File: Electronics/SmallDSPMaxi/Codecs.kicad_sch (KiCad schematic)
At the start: 72 parts, among them J1 IDC Header

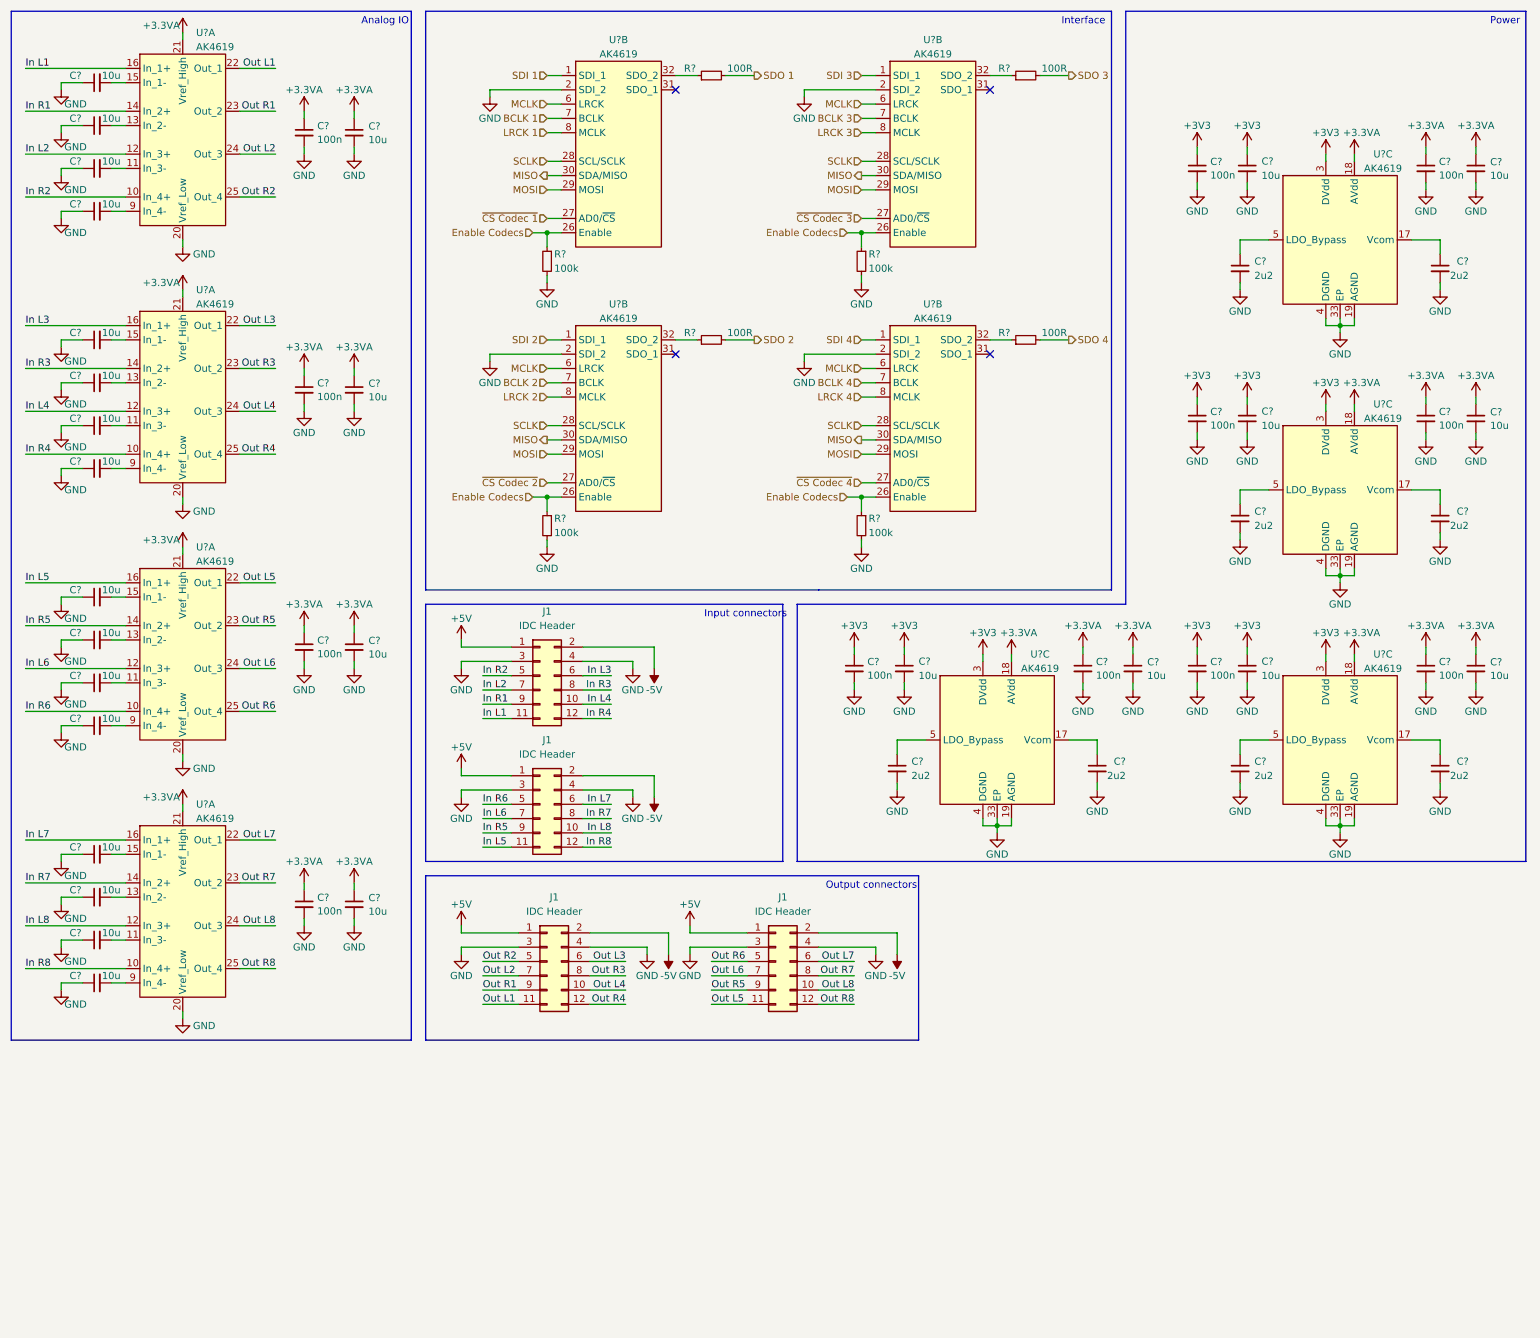
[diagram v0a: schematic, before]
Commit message: Finishes SmallDSP Maxi plus the fitting In- and Output Boards
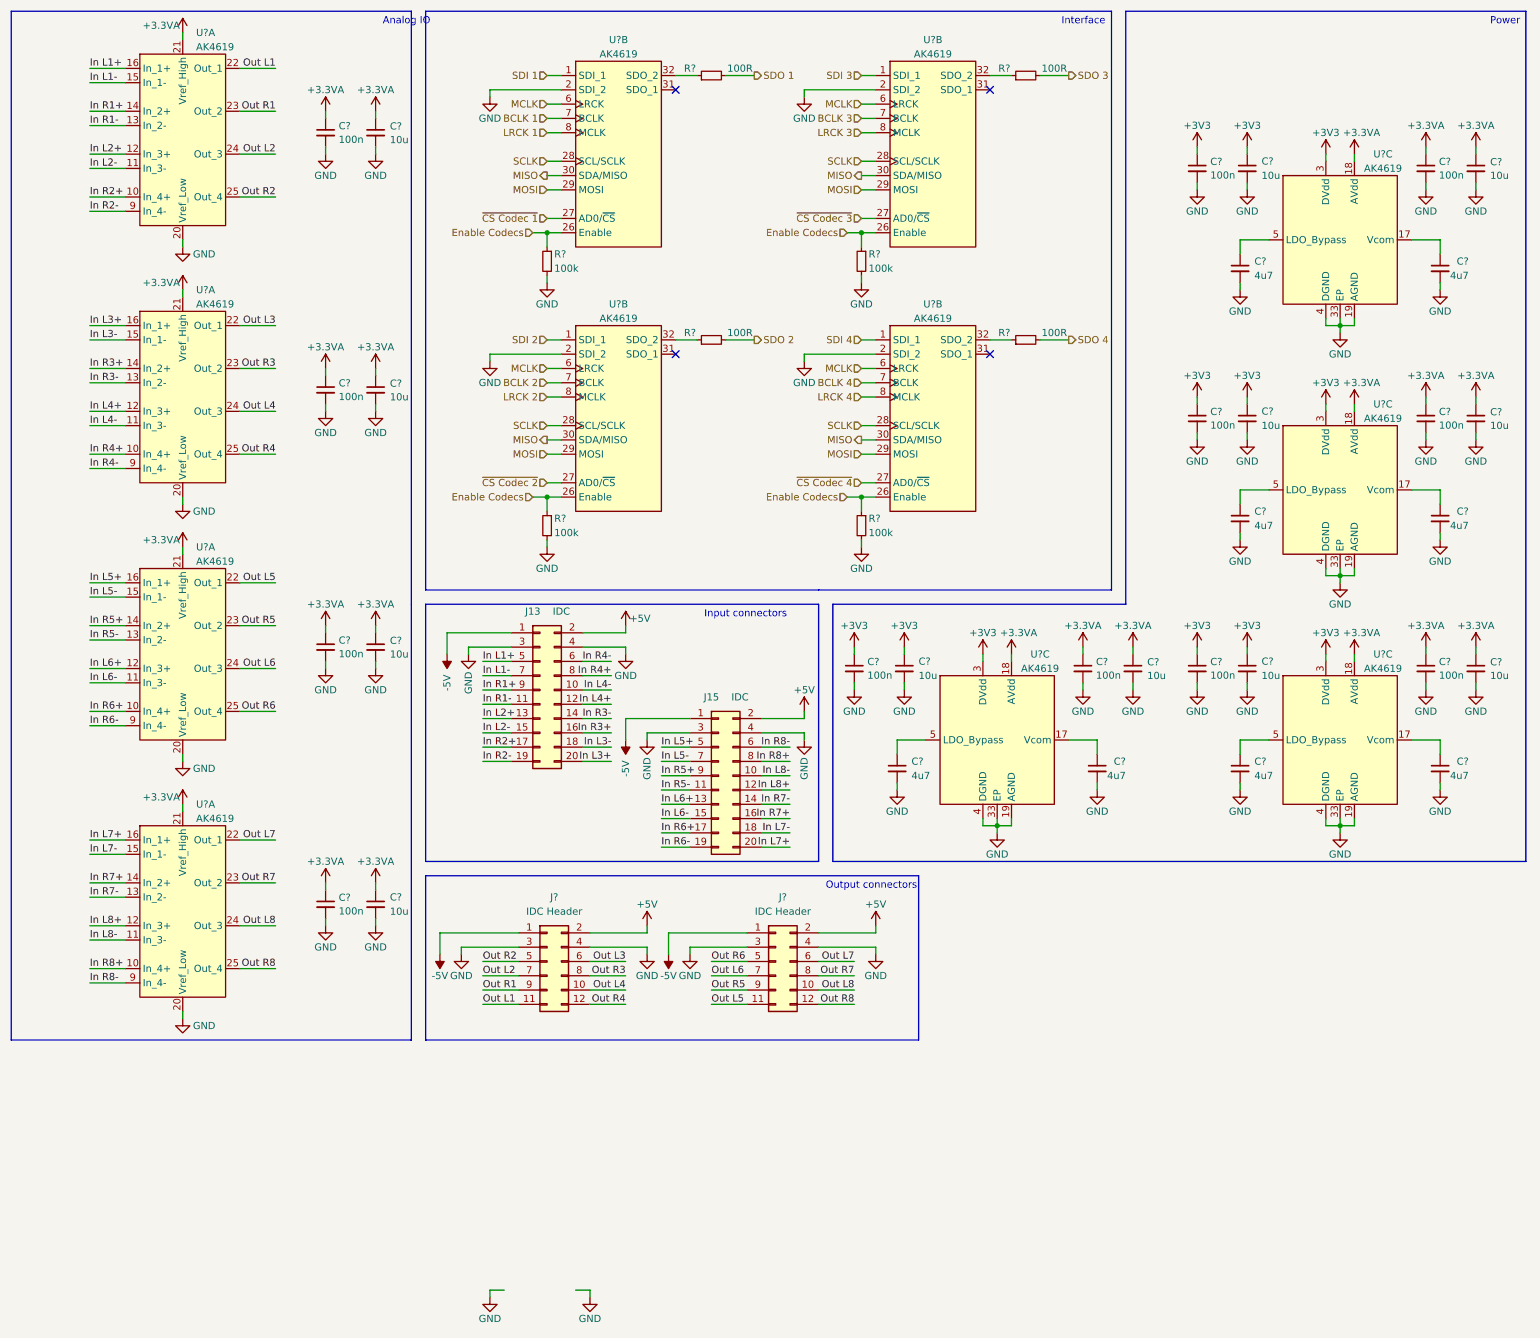
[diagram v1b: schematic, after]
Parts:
- removed C? (x16): 10u, Capacitor_SMD:C_1206_3216Metric, symbol Device:C_Small
- removed J1 (x2): IDC Header, Connector_IDC:IDC-Header_2x06_P2.54mm_Vertical, symbol Connector_Generic:Conn_02x06_Odd_Even
- added J13, J15: IDC, Connector_IDC:IDC-Header_2x10_P2.54mm_Vertical, symbol Connector_Generic:Conn_02x10_Odd_Even
- C? (x12): JLC Part Number C307331 -> (none); LCSC Part # (none) -> C307331
- C? (x12): JLC Part Number C96446 -> (none); LCSC Part # (none) -> C96446
- C? (x8): value 2u2 -> 4u7; footprint Capacitor_SMD:C_0805_2012Metric -> Capacitor_SMD:C_0603_1608Metric; JLC Part Number C377773 -> (none); LCSC Part # (none) -> C19666; Notes (none) -> -50%@3.3V and 0Vrms; Part Number CL21A225KBQNNNE -> CL10A475KO8NNNC
- J? (x2): renamed from J1; JLC Part Number - -> (none); LCSC Part # (none) -> -
- R? (x4): JLC Part Number C25076 -> (none); LCSC Part # (none) -> C25076
- R? (x4): JLC Part Number C25741 -> (none); LCSC Part # (none) -> C25741
- U? (x12): LCSC Part # (none) -> -
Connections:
- net +5V: now also J?.2 (Pin_2), J?.2 (Pin_2), J13.2 (Pin_2), J15.2 (Pin_2); no longer J?.1 (Pin_1), J?.1 (Pin_1)
- net -5V: now also J?.1 (Pin_1), J?.1 (Pin_1), J13.1 (Pin_1), J15.1 (Pin_1); no longer J?.2 (Pin_2), J?.2 (Pin_2)
- net GND: now also J13.3 (Pin_3), J13.4 (Pin_4), J15.3 (Pin_3), J15.4 (Pin_4)
- net In L6-: now reaches U?.11 (In_3-)
- net In L6-: now also J15.15 (Pin_15)
- net In R5-: now reaches U?.13 (In_2-)
- net In R5-: now also J15.11 (Pin_11)
- net In L5-: now reaches U?.15 (In_1-)
- net In L5-: now also J15.7 (Pin_7)
- net In R6-: now reaches U?.9 (In_4-)
- net In R6-: now also J15.19 (Pin_19)
- net In L2-: now reaches U?.11 (In_3-)
- net In L2-: now also J13.15 (Pin_15)
- net In L1-: now reaches U?.15 (In_1-)
- net In L1-: now also J13.7 (Pin_7)
- net In L8-: now reaches U?.11 (In_3-)
- net In L8-: now also J15.10 (Pin_10)
- net In R1-: now reaches U?.13 (In_2-)
- net In R1-: now also J13.11 (Pin_11)
- net In R2-: now reaches U?.9 (In_4-)
- net In R2-: now also J13.19 (Pin_19)
- net In L3-: now reaches U?.15 (In_1-)
- net In L3-: now also J13.18 (Pin_18)
- net In R7-: now reaches U?.13 (In_2-)
- net In R7-: now also J15.14 (Pin_14)
- net In R3-: now reaches U?.13 (In_2-)
- net In R3-: now also J13.14 (Pin_14)
- net In R8-: now reaches U?.9 (In_4-)
- net In R8-: now also J15.6 (Pin_6)
- net In L4-: now reaches U?.11 (In_3-)
- net In L4-: now also J13.10 (Pin_10)
- net In R4-: now reaches U?.9 (In_4-)
- net In R4-: now also J13.6 (Pin_6)
- net In L7-: now reaches U?.15 (In_1-)
- net In L7-: now also J15.18 (Pin_18)
- net In L1 renamed In L1+
- net In L1+: now also J13.5 (Pin_5)
- net In L2 renamed In L2+
- net In L2+: now also J13.13 (Pin_13)
- net In L3 renamed In L3+
- net In L3+: now also J13.20 (Pin_20)
- net In L4 renamed In L4+
- net In L4+: now also J13.12 (Pin_12)
- net In L5 renamed In L5+
- net In L5+: now also J15.5 (Pin_5)
- net In L6 renamed In L6+
- net In L6+: now also J15.13 (Pin_13)
- net In L7 renamed In L7+
- net In L7+: now also J15.20 (Pin_20)
- net In L8 renamed In L8+
- net In L8+: now also J15.12 (Pin_12)
- net In R1 renamed In R1+
- net In R1+: now also J13.9 (Pin_9)
- net In R2 renamed In R2+
- net In R2+: now also J13.17 (Pin_17)
- net In R3 renamed In R3+
- net In R3+: now also J13.16 (Pin_16)
- net In R4 renamed In R4+
- net In R4+: now also J13.8 (Pin_8)
- net In R5 renamed In R5+
- net In R5+: now also J15.9 (Pin_9)
- net In R6 renamed In R6+
- net In R6+: now also J15.17 (Pin_17)
- net In R7 renamed In R7+
- net In R7+: now also J15.16 (Pin_16)
- net In R8 renamed In R8+
- net In R8+: now also J15.8 (Pin_8)
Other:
- moved on the sheet: C?

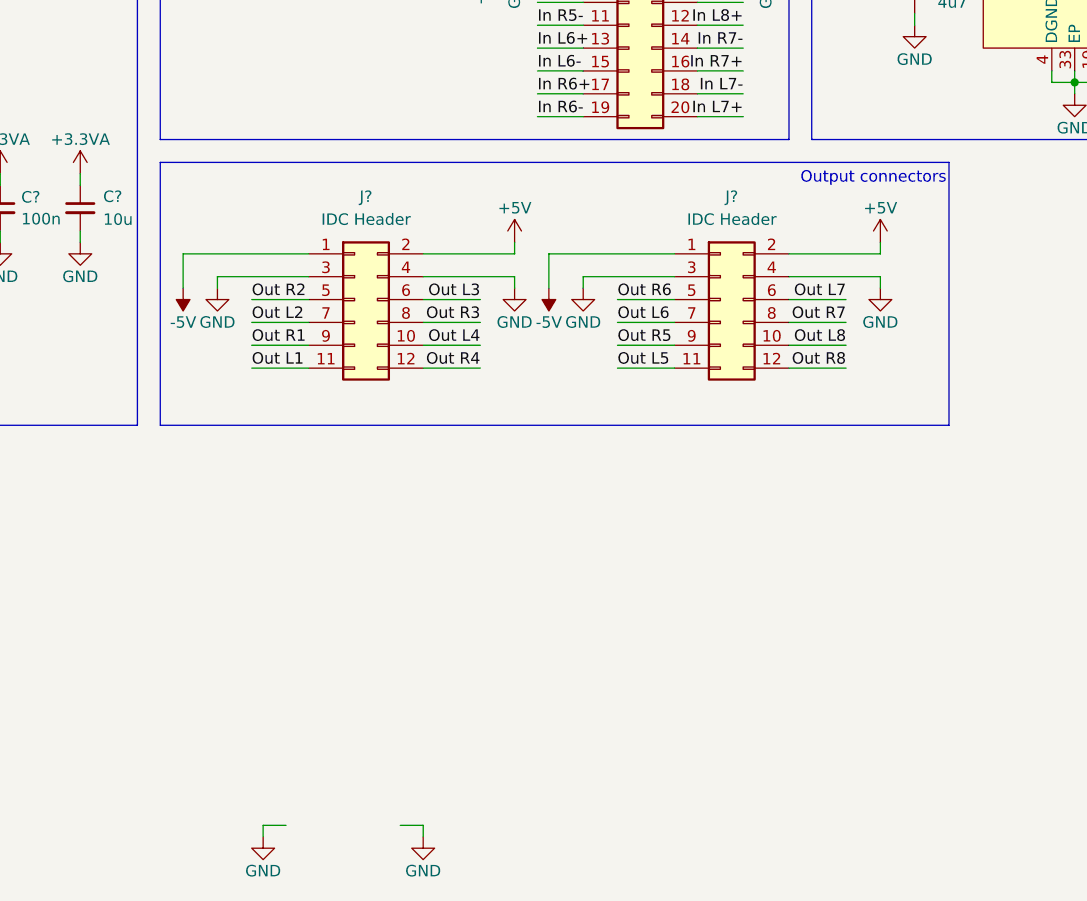
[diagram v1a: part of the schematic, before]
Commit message: replaces 12pin IDC out header with 14pin one because of better availability.
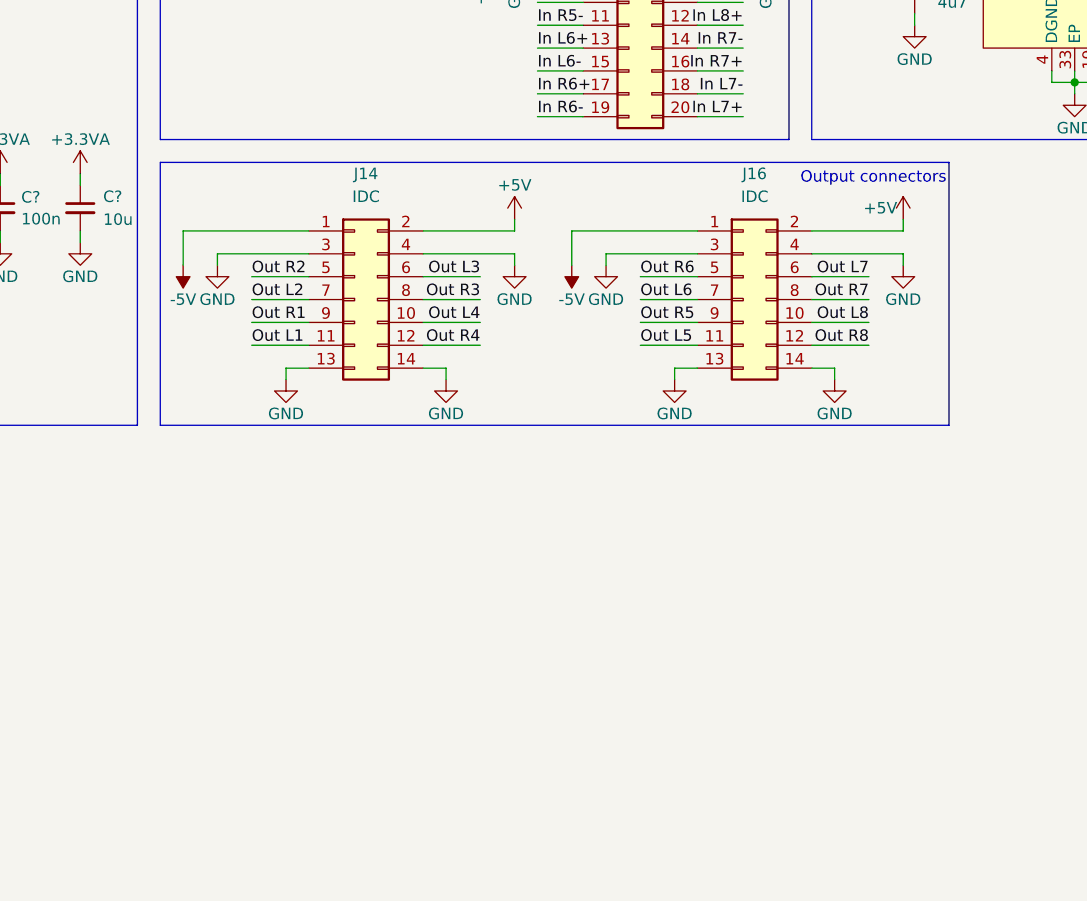
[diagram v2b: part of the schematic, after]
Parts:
- removed J? (x2): IDC Header, Connector_IDC:IDC-Header_2x06_P2.54mm_Vertical, symbol Connector_Generic:Conn_02x06_Odd_Even
- added J14, J16: IDC, Connector_IDC:IDC-Header_2x07_P2.54mm_Vertical, symbol Connector_Generic:Conn_02x07_Odd_Even
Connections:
- net +5V: now also J14.2 (Pin_2), J16.2 (Pin_2)
- net -5V: now also J14.1 (Pin_1), J16.1 (Pin_1)
- net GND: now also J14.13 (Pin_13), J14.14 (Pin_14), J14.3 (Pin_3), J14.4 (Pin_4), J16.13 (Pin_13), J16.14 (Pin_14), J16.3 (Pin_3), J16.4 (Pin_4)
- net Out L1: now also J14.11 (Pin_11)
- net Out L2: now also J14.7 (Pin_7)
- net Out L3: now also J14.6 (Pin_6)
- net Out L4: now also J14.10 (Pin_10)
- net Out L5: now also J16.11 (Pin_11)
- net Out L6: now also J16.7 (Pin_7)
- net Out L7: now also J16.6 (Pin_6)
- net Out L8: now also J16.10 (Pin_10)
- net Out R1: now also J14.9 (Pin_9)
- net Out R2: now also J14.5 (Pin_5)
- net Out R3: now also J14.8 (Pin_8)
- net Out R4: now also J14.12 (Pin_12)
- net Out R5: now also J16.9 (Pin_9)
- net Out R6: now also J16.5 (Pin_5)
- net Out R7: now also J16.8 (Pin_8)
- net Out R8: now also J16.12 (Pin_12)

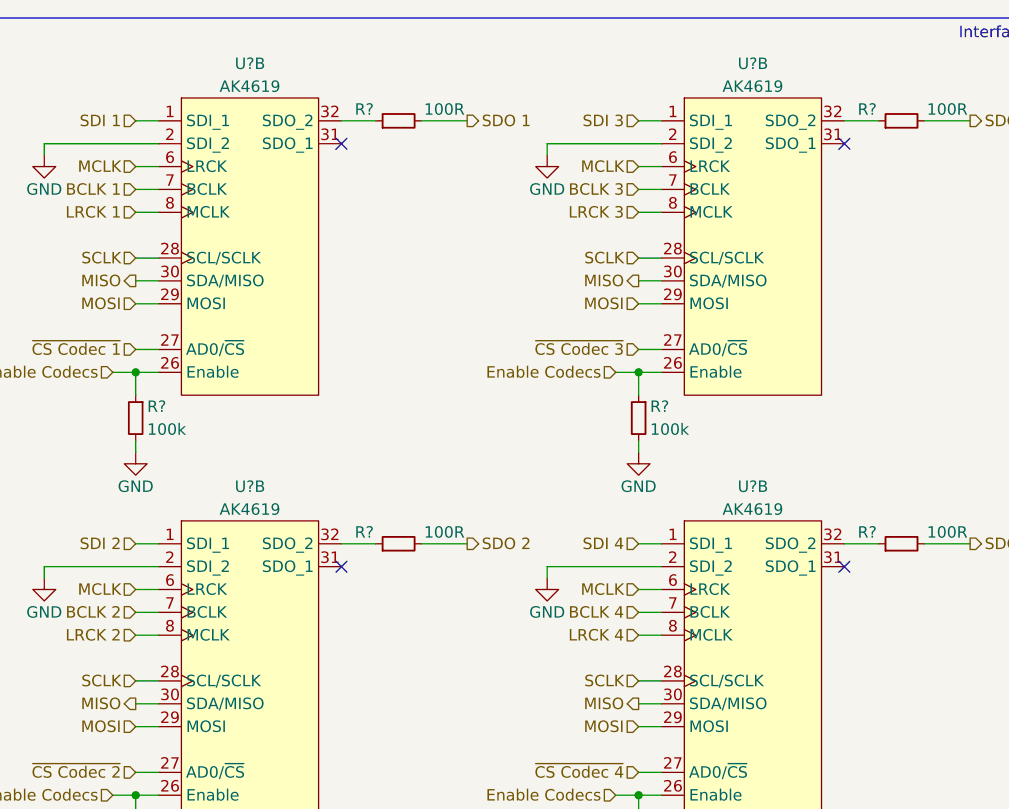
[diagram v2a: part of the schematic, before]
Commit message: Fixes schematic mistakes, like incorrect routin of clock to codecs
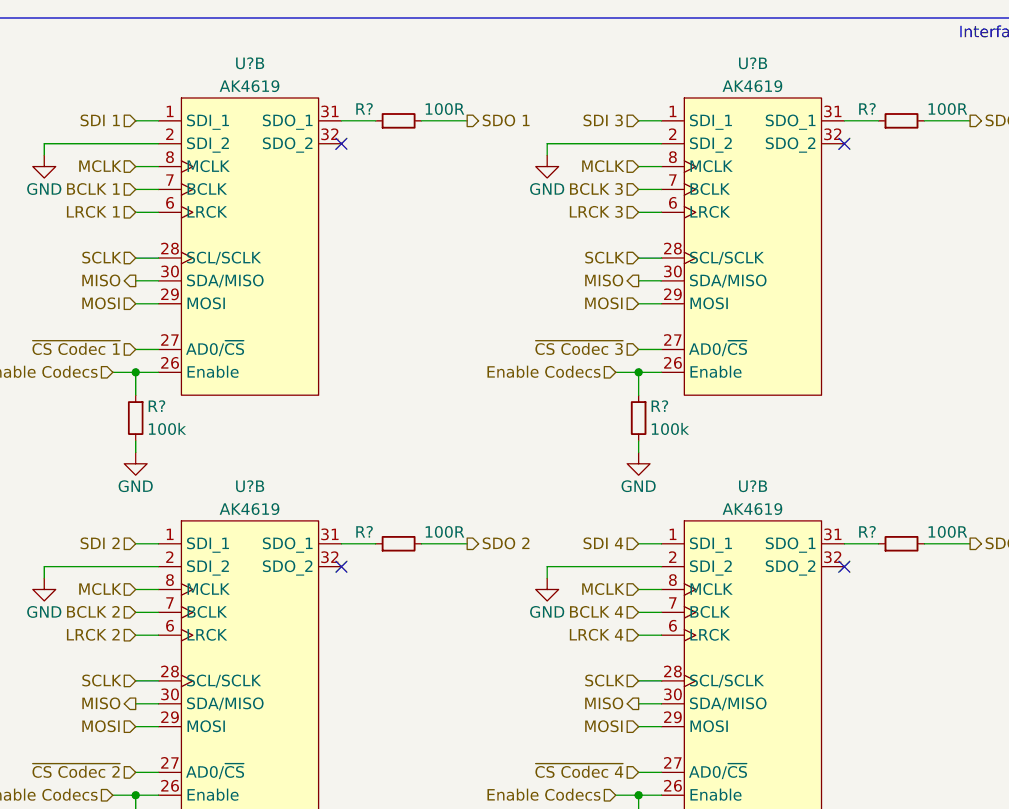
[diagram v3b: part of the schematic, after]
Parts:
- U? (x12): Part Number AK4619 -> AK4619VN
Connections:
- net LRCK 1: now also U?.6 (LRCK); no longer U?.8 (MCLK)
- net LRCK 2: now also U?.6 (LRCK); no longer U?.8 (MCLK)
- net LRCK 3: now also U?.6 (LRCK); no longer U?.8 (MCLK)
- net LRCK 4: now also U?.6 (LRCK); no longer U?.8 (MCLK)
- net MCLK: now also U?.8 (MCLK), U?.8 (MCLK), U?.8 (MCLK), U?.8 (MCLK); no longer U?.6 (LRCK), U?.6 (LRCK), U?.6 (LRCK), U?.6 (LRCK)
- net at R?.1: now also U?.31 (SDO_1); no longer U?.32 (SDO_2) (x3)
- net at U?.31 (SDO_1): now also R?.1
- net at U?.32 (SDO_2): no longer R?.1
